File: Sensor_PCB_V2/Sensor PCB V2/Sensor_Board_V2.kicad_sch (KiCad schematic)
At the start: 35 parts

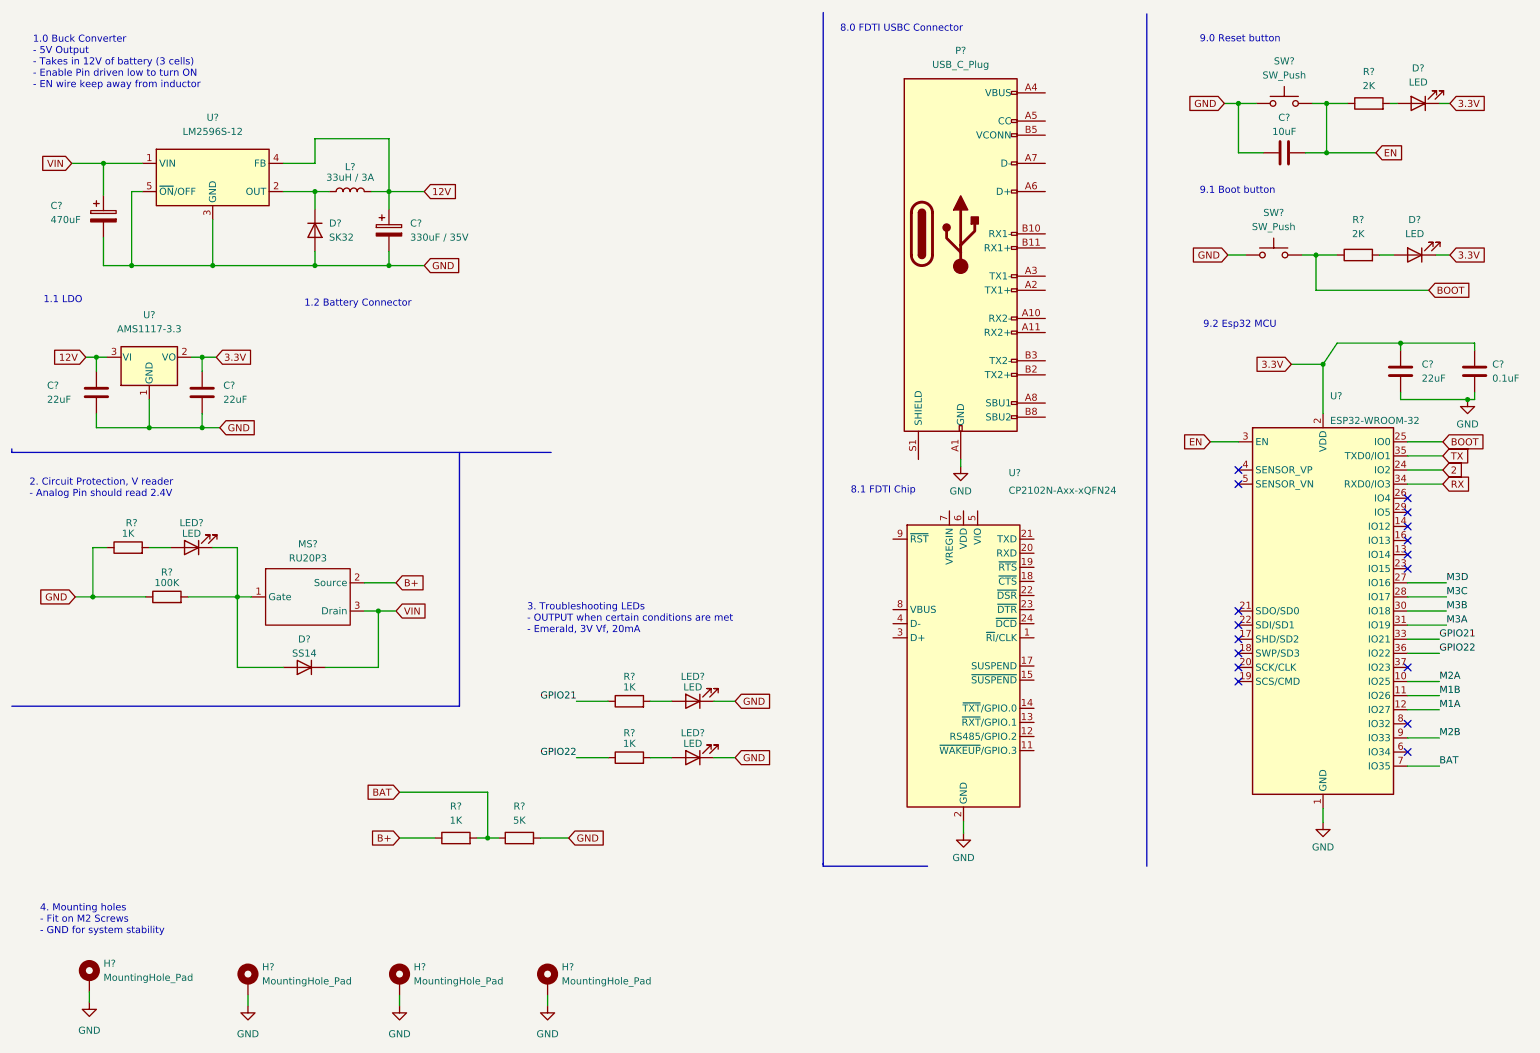
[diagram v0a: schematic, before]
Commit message: Added new Sch. files for PCB Version 2 - Circuit Protection - Added a 5V power supply - Added Circuit protection - Added additional bypass capacitors for EN - Removed troubleshooting LEDs
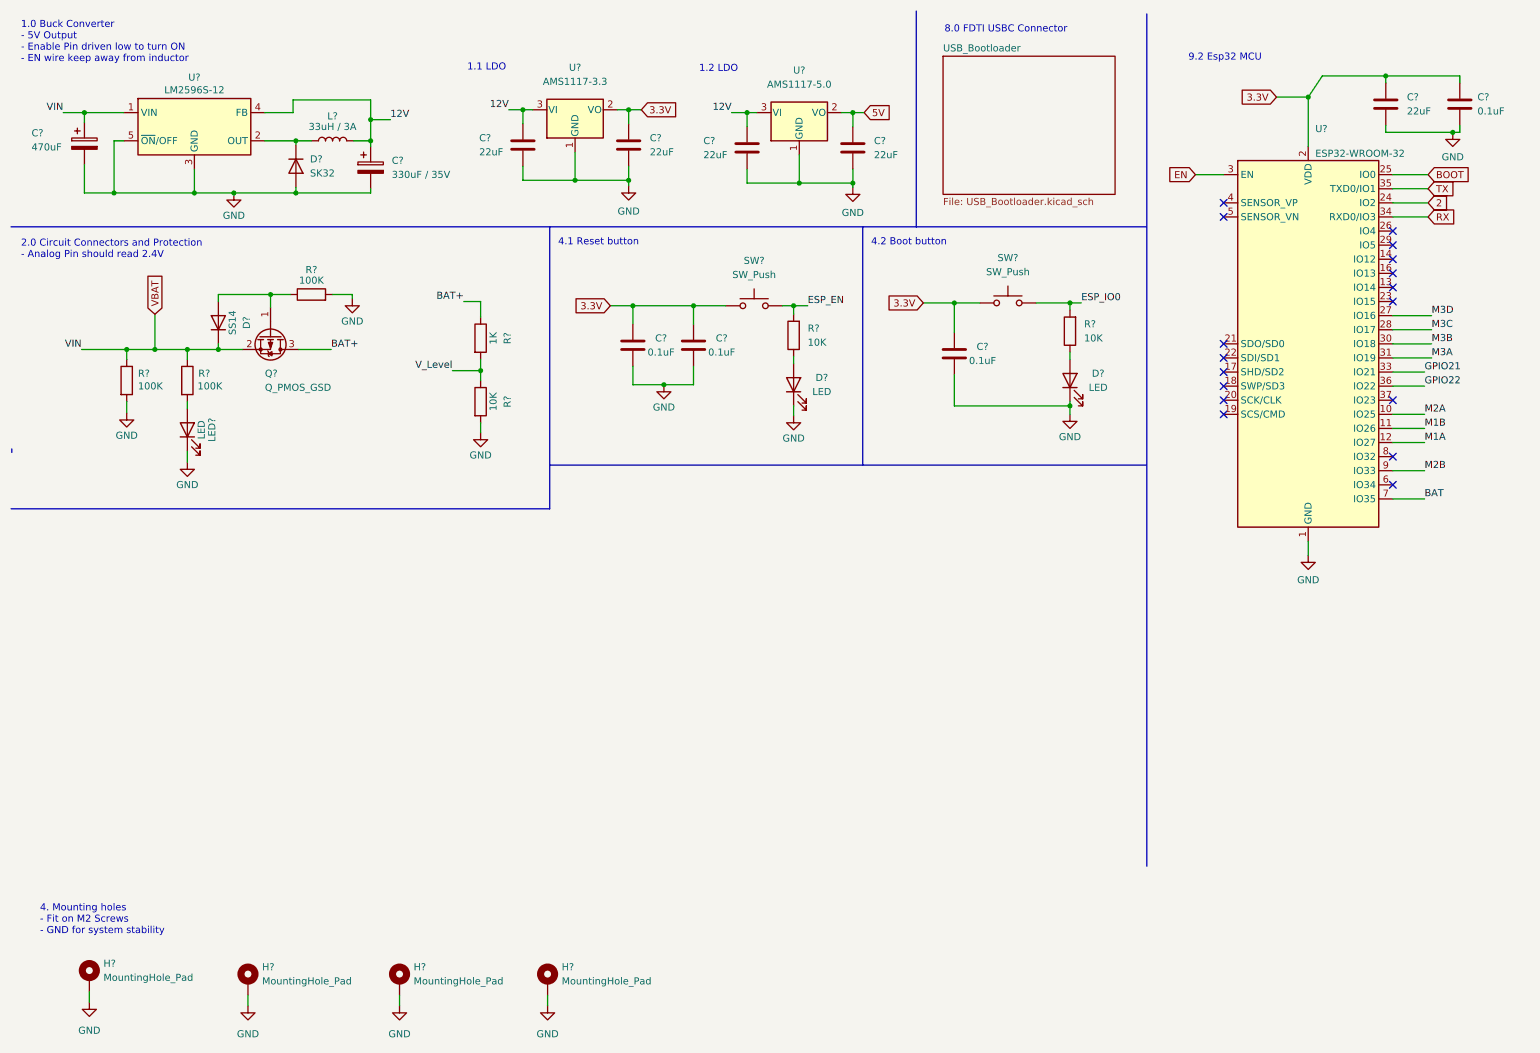
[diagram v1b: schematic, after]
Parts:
- removed C?: 10uF, Capacitor_SMD:C_0603_1608Metric, symbol Device:C
- removed D?: SS14, Diode_SMD:D_SMA, symbol Device:D
- removed D? (x2): LED, symbol Device:LED
- removed LED? (x3): LED, LED_SMD:LED_0603_1608Metric, symbol Device:LED
- removed MS?: RU20P3, Package_TO_SOT_SMD:SOT-23, symbol RU20P3B:RU20P3
- removed P?: USB_C_Plug, symbol Connector:USB_C_Plug
- removed R?: 5K, Resistor_SMD:R_0603_1608Metric, symbol Device:R
- removed R? (x4): 1K, Resistor_SMD:R_0603_1608Metric, symbol Device:R
- removed R?: 100K, Resistor_SMD:R_0603_1608Metric, symbol Device:R
- removed R? (x2): 2K, Resistor_SMD:R_0603_1608Metric, symbol Device:R
- removed SW? (x2): SW_Push, Button_Switch_SMD:SW_SPST_Omron_B3FS-100xP, symbol Switch:SW_Push
- removed U?: CP2102N-Axx-xQFN24, Package_DFN_QFN:QFN-24-1EP_4x4mm_P0.5mm_EP2.6x2.6mm, symbol Interface_USB:CP2102N-Axx-xQFN24
- added C? (x3): 0.1uF, Capacitor_SMD:C_0603_1608Metric, symbol Device:C
- added C? (x2): 22uF, Capacitor_SMD:C_0603_1608Metric, symbol Device:C
- added D?: SS14, Diode_SMD:D_SMA, symbol Device:D
- added D? (x2): LED, symbol Device:LED
- added LED?: LED, LED_SMD:LED_0603_1608Metric, symbol Device:LED
- added Q?: Q_PMOS_GSD, symbol Device:Q_PMOS_GSD
- added R? (x3): 10K, Resistor_SMD:R_0603_1608Metric, symbol Device:R
- added R?: 100K, symbol Device:R
- added R? (x2): 100K, Resistor_SMD:R_0603_1608Metric, symbol Device:R
- added R?: 1K, Resistor_SMD:R_0603_1608Metric, symbol Device:R
- added SW? (x2): SW_Push, Button_Switch_SMD:SW_SPST_Omron_B3FS-100xP, symbol Switch:SW_Push
- added U?: AMS1117-5.0, Package_TO_SOT_SMD:SOT-223-3_TabPin2, symbol Regulator_Linear:AMS1117-5.0
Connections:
- net 12V: now also C?.1, U?.3 (VI)
- net 3.3V: now also C?.1, C?.1, C?.1, SW?.1, SW?.1
- net GND: now also C?.2, C?.2, C?.2, C?.2, C?.2, D?.1 (K), D?.1 (K), LED?.1 (K), R?.2, R?.2, R?.2, U?.1 (GND)
- net VIN renamed VBAT
- net VBAT: now also D?.1 (K), Q?.2 (S), R?.1, R?.1
- new net: D?.2 (A), R?.1 (x2)
- new net: D?.2 (A), Q?.1 (G), R?.1
- new net: LED?.2 (A), R?.2
- new net 5V: C?.1, U?.2 (VO)
- new net BAT+: Q?.3 (D), R?.1
- new net ESP_EN: R?.2, SW?.2
- new net ESP_IO0: R?.2, SW?.2
- new net V_Level: R?.1, R?.2
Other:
- added sheet USB_Bootloader (USB_Bootloader.kicad_sch)
- note added: "1.0 Buck Converter - 5V Output - Enable Pin driven low to turn ON - EN wire keep away from inductor"
- note added: "1.2 LDO"
- note added: "2.0 Circuit Connectors and Protection - Analog Pin should read 2.4V"
- note added: "4.1 Reset button"
- note added: "4.2 Boot button"
- note removed: "1.0 Buck Converter - 5V Output - Takes in 12V of battery (3 cells) - Enable Pin driven low to turn ON - EN wire keep away from inductor"
- note removed: "1.2 Battery Connector"
- note removed: "2. Circuit Protection, V reader - Analog Pin should read 2.4V"
- note removed: "3. Troubleshooting LEDs - OUTPUT when certain conditions are met - Emerald, 3V Vf, 20mA"
- note removed: "8.1 FDTI Chip"
- note removed: "9.0 Reset button"
- note removed: "9.1 Boot button"
- moved on the sheet: C?, D?, L?, U?
